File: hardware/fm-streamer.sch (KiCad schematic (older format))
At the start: 35 parts

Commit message: schematics nominally finished, moving on to PCB
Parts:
- removed C?: 0.1u, symbol Device:C_Small
- removed C? (x5): 10u, symbol Device:C_Small
- removed C? (x2): 47u, symbol Device:CP_Small
- removed R? (x6): 10k, symbol Device:R_Small
- removed U?: ESP32-DEVKITC-32D, MODULE_ESP32-DEVKITC-32D, symbol ESP32-DEVKITC-32D:ESP32-DEVKITC-32D
- removed U?: UDA1334ATS, Package_SO:SSOP-16_4.4x5.2mm_P0.65mm, symbol Audio:UDA1334ATS
- added C1: 0.1u, Capacitor_SMD:C_0402_1005Metric, symbol Device:C_Small
- added C10, C11, C17, C4, C5, C6, C7, C8, C9: 22n, Capacitor_SMD:C_0402_1005Metric, symbol Device:C_Small
- added C12, C14, C16, C19, C2, C20, C22, C23, C3: 10u, Capacitor_SMD:C_0603_1608Metric, symbol Device:C_Small
- added J1: USB_A, Connector_USB:USB_A_Molex_105057_Vertical, symbol Connector:USB_A
- added L1: 120n, Inductor_SMD:L_0603_1608Metric, symbol Device:L_Small
- added R1, R14, R2: 0, Resistor_SMD:R_0402_1005Metric, symbol Device:R_Small
- added R10, R11, R17, R7, R8, R9: 100, Resistor_SMD:R_0402_1005Metric, symbol Device:R_Small
- added R15, R16, R20, R21: 10k, Resistor_SMD:R_0402_1005Metric, symbol Device:R_Small
- added TP1: TestPoint, TestPoint:TestPoint_Plated_Hole_D2.0mm, symbol Connector:TestPoint
- added U1: ESP32_DevKit_V1_DOIT, esp32_devkit_v1_doit:esp32_devkit_v1_doit, symbol esp32_devkit_v1_doit:ESP32_DevKit_V1_DOIT
- added U2: PCM1772PWR, footprints:PCM1772PWR, symbol 2021-05-02_19-16-46:PCM1772PWR
- C13, C15, C18: renamed from C?; footprint (none) -> Capacitor_SMD:C_0402_1005Metric; MFG (none) -> Murata; MPN (none) -> GCM155R71C104KA55J
- C21: renamed from C?; footprint (none) -> Capacitor_SMD:C_0603_1608Metric; MFG (none) -> Murata; MPN (none) -> GRT188C81A106ME13D
- R12, R13, R18, R19, R22, R23, R24, R25, R26, R27, R3, R4, R5, R6: renamed from R?; footprint (none) -> Resistor_SMD:R_0402_1005Metric
- U3: renamed from U?; footprint QFN-20-3X3MM -> SI4721:QFN-20-3X3MM; MFG (none) -> Silicon Labs; MPN (none) -> SI4721-B20-GM
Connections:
- net +3V3: now also R13.2, C14.1, C17.1, C3.2, U1.16 (3V3), U2.12 (VCC1); no longer R13.1
- net AUDIO_L: now also R27.1, C23.1; no longer R26.1
- net AUDIO_R: now also R26.1, C22.2; no longer R27.1
- net GND: now also U3.2 (FMI), C1.2, C10.2, C11.2, C12.2, C14.2, C16.2, C17.2, C2.2, C22.1, C23.2, C3.1, C4.2, C5.2, C6.2, C7.2, C8.2, C9.2, J1.4 (GND), J1.5 (Shield), L1.2, R1.1, R15.2, R16.2, R17.2, R2.1, R20.2, R21.2, U1.14 (GND), U1.17 (GND), U2.5 (AGND1), U2.6 (AGND2)
- net I2C_SCK: now also U1.29 (IO22)
- net I2C_SDA: now also U1.26 (IO21)
- net I2S_DATA: now also C5.1, U2.2 (DATA)
- net I2S_DCLK: now also C6.1, U2.3 (BCK)
- net I2S_WCLK: now also C4.1, U2.1 (LRCK)
- net RADIO_~RST~: now also U1.8 (IO25)
- net at U3.18 (GPO2/~INT): now also R21.1
- net at U3.19 (GPO1): now also R20.1
- net at U3.4 (TXO): now also L1.1, R14.1, TP1.1
- net RADIO_REFCLK: now reaches U3.9 (RCLK)
- net RADIO_REFCLK: now also C7.1, R7.1
- net at C13.1: now also R13.1, C12.1, U2.11 (VCC2); no longer R13.2
- net at R25.2, R27.2: now also C20.1
- net at R24.1, R26.2: now also C19.1
- net I2S_WCLK_R: now reaches R4.2
- net I2S_WCLK_R: now also U1.22 (IO17)
- net I2S_DATA_R: now reaches R5.2
- net I2S_DATA_R: now also U1.21 (IO16)
- net I2S_DCLK_R: now reaches R6.2
- net I2S_DCLK_R: now also U1.20 (IO4)
- new net: J1.2 (D-), R2.2
- new net: J1.3 (D+), R1.2
- new net: R17.1, U2.10 (AIN)
- new net: C16.1, U2.7 (VCOM)
- new net: C19.2, U2.8 (VOUTR)
- new net: C20.2, U2.9 (VOUTL)
- new net +5V: C1.1, C2.1, J1.1 (VBUS), U1.15 (VIN)
- new net ANTENNA: R14.2
- new net DAC_CLK_R: R8.2, U1.28 (TXD0/IO1)
- new net DAC_REFCLK: C8.1, R8.1, U2.16 (SCKI)
- new net DAC_~RST~: R15.1, U1.10 (IO27), U2.4 (*PD)
- new net RAD_CLK_R: R7.2, U1.27 (RXD0/IO3)
- new net SPI_CLK: C10.1, R10.1, U2.14 (MC)
- new net SPI_CLK_R: R10.2, U1.24 (IO18)
- new net SPI_CS: C11.1, R11.1
- new net SPI_CS_R: R11.2, U1.23 (IO5)
- new net SPI_MOSI: C9.1, R9.1, U2.13 (MD)
- new net SPI_MOSI_R: R9.2, U1.30 (IO23)
- new net SPI_~CS~: R16.1, U2.15 (*MS)
- no-connect marks 1 -> 3
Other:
- note added: "Testpoint for optional wire antenna"
- note added: "http://esp32.net/images/DOIT/ESP32-DevKit-V1/DOIT_ESP32-DevKit_Schematic.pdf"
- moved on the sheet: C13, C15, C18, C21, R12, R13, R18, R19, R22, R23, R24, R25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

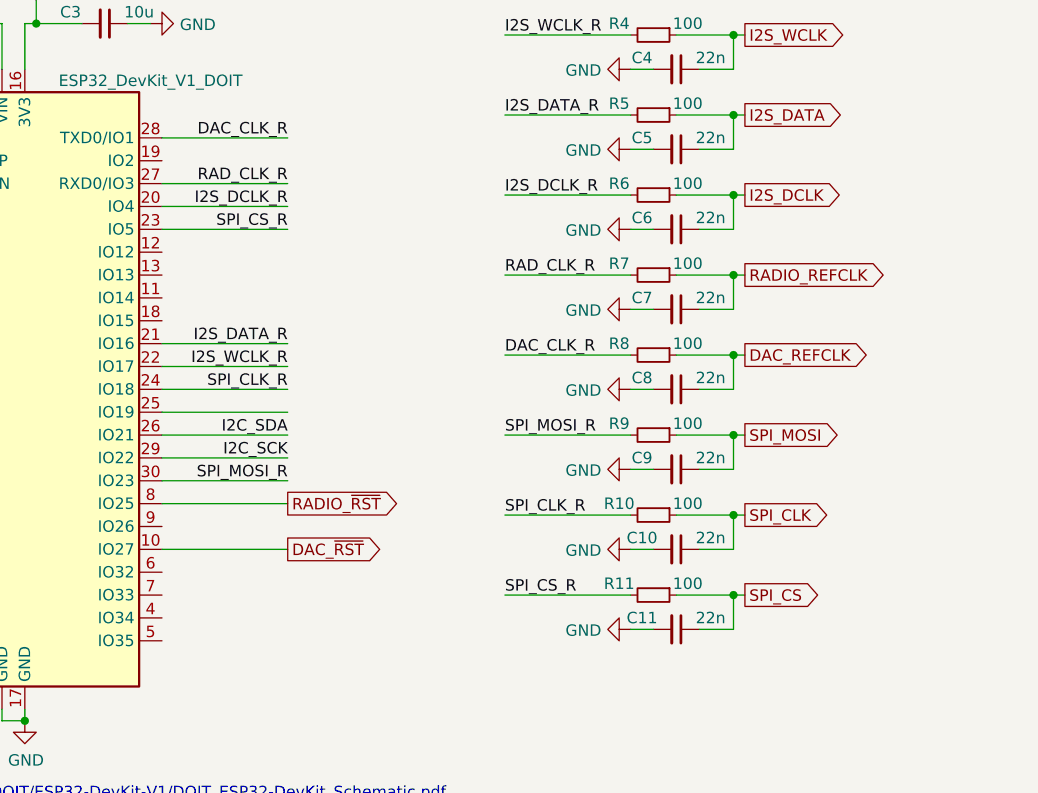
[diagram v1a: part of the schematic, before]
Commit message: rough placement and routing complete, needs cleanup
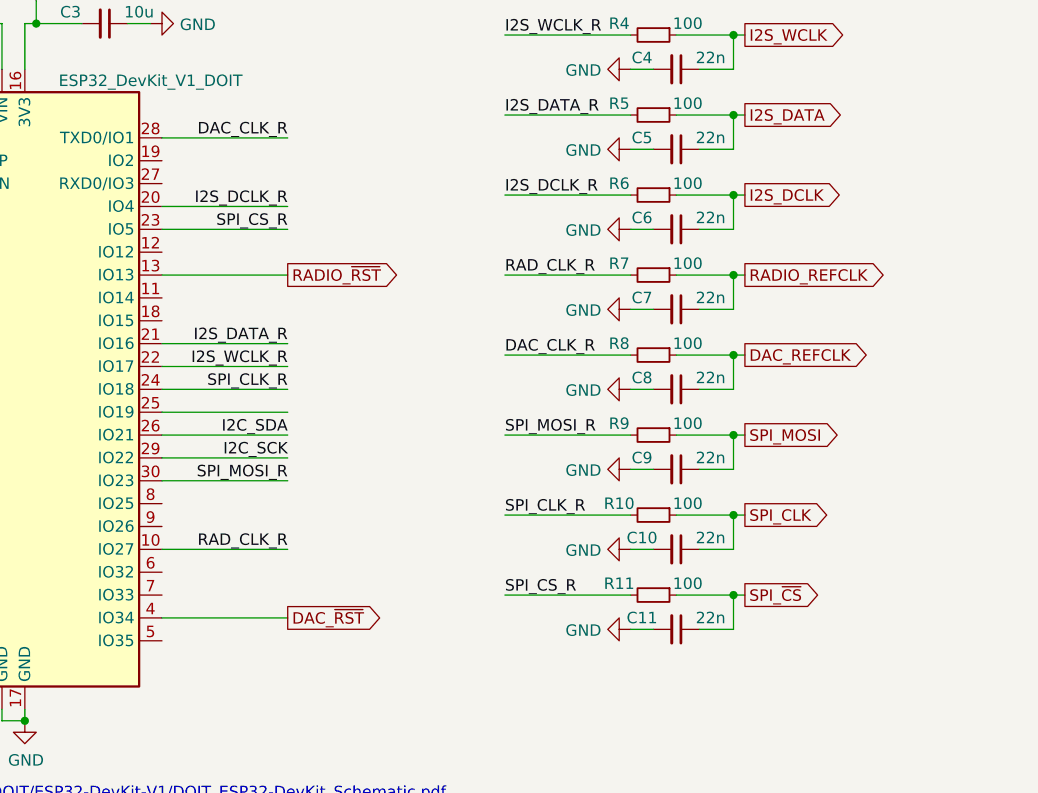
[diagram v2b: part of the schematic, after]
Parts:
- TP1: footprint TestPoint:TestPoint_Plated_Hole_D2.0mm -> TestPoint:TestPoint_THTPad_D2.0mm_Drill1.0mm
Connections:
- net SPI_CS is gone; now on net SPI_~CS~: C11.1, R11.1
- net DAC_~RST~: now also U1.4 (IO34); no longer U1.10 (IO27)
- net RADIO_~RST~: now also U1.13 (IO13); no longer U1.8 (IO25)
- net RAD_CLK_R: now also U1.10 (IO27); no longer U1.27 (RXD0/IO3)
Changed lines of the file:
@@
 Text GLabel 7400 2950 2    50   BiDi ~ 0
 I2C_SDA
-Text GLabel 5400 5350 2    50   Output ~ 0
+Text GLabel 5400 4350 2    50   Output ~ 0
 RADIO_~RST~
 $Comp
@@
 F 0 "TP1" H 10108 3272 50  0000 L CNN
 F 1 "TestPoint" H 10108 3227 50  0001 L CNN
-F 2 "TestPoint:TestPoint_Plated_Hole_D2.0mm" H 10250 3200 50  0001 C CNN
+F 2 "TestPoint:TestPoint_THTPad_D2.0mm_Drill1.0mm" H 10250 3200 50  0001 C CNN
 F 3 "~" H 10250 3200 50  0001 C CNN
 F 4 "~" H 10050 3200 50  0001 C CNN "MFG"
@@
 	4850 5150 5400 5150
 Wire Wire Line
-	5400 5350 4850 5350
+	5400 4350 4850 4350
 Wire Wire Line
 	6900 4000 6350 4000
@@
 Text Label 6350 4350 0    50   ~ 0
 RAD_CLK_R
-Text Label 5400 3950 2    50   ~ 0
+Text Label 5400 5550 2    50   ~ 0
 RAD_CLK_R
 Wire Wire Line
-	5400 3950 4850 3950
+	5400 5550 4850 5550
 Connection ~ 7350 4350
 Wire Wire Line
@@
 	7350 5750 7400 5750
 Text GLabel 7400 5750 2    50   Output ~ 0
-SPI_CS
+SPI_~CS~
 Text Label 5400 5250 2    50   ~ 0
 SPI_MOSI_R
@@
 Text Label 5400 4150 2    50   ~ 0
 SPI_CS_R
-Text GLabel 5400 5550 2    50   Output ~ 0
+Text GLabel 5400 5850 2    50   Output ~ 0
 DAC_~RST~
 Wire Wire Line
-	4850 5550 5400 5550
+	4850 5850 5400 5850
 $Comp
 L Device:C_Small C19

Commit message: cleaning up routing
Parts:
- added R28, R29, R30: 0, Resistor_SMD:R_0402_1005Metric, symbol Device:R_Small
- J1: footprint Connector_USB:USB_A_Molex_105057_Vertical -> Connector_USB:USB_A_Plug_Molex_0480371000_90_deg_mount
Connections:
- net DAC_CLK_R: now also U1.4 (IO34); no longer U1.28 (TXD0/IO1)
- net DAC_~RST~: now also U1.26 (IO21); no longer U1.4 (IO34)
- net I2C_SDA: now also U1.9 (IO26); no longer U1.26 (IO21)
- net I2S_DATA: now also R29.2; no longer U2.2 (DATA)
- net I2S_DATA_R: now also U1.24 (IO18); no longer U1.21 (IO16)
- net I2S_DCLK: now also R28.2; no longer U2.3 (BCK)
- net I2S_DCLK_R: now also U1.21 (IO16); no longer U1.20 (IO4)
- net I2S_WCLK: now also R30.2; no longer U2.1 (LRCK)
- net RAD_CLK_R: now also U1.8 (IO25); no longer U1.10 (IO27)
- net SPI_CLK_R: now also U1.6 (IO32); no longer U1.24 (IO18)
- net SPI_CS_R: now also U1.5 (IO35); no longer U1.23 (IO5)
- net SPI_MOSI_R: now also U1.7 (IO33); no longer U1.30 (IO23)
- net I2C_SCK renamed I2C_SCL
- net I2C_SCL: now also U1.10 (IO27); no longer U1.29 (IO22)
- new net: R30.1, U2.1 (LRCK)
- new net: R29.1, U2.2 (DATA)
- new net: R28.1, U2.3 (BCK)
- no-connect marks 3 -> 10
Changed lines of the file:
@@
 	9550 7200 9550 7150
 Wire Wire Line
-	11500 6150 10700 6150
-Wire Wire Line
-	11500 6350 10700 6350
-Wire Wire Line
-	11500 6250 10700 6250
+	11500 6150 11300 6150
+Wire Wire Line
+	11500 6350 11300 6350
+Wire Wire Line
+	11500 6250 11300 6250
 $Comp
 L Device:R_Small R13
@@
 I2C_SDA
 Text GLabel 11250 3850 0    50   BiDi ~ 0
-I2C_SCK
+I2C_SCL
 Wire Wire Line
 	11250 3950 11800 3950
@@
 	7100 3300 7350 3300
 Text GLabel 7400 2850 2    50   BiDi ~ 0
-I2C_SCK
+I2C_SCL
 Text GLabel 7400 2950 2    50   BiDi ~ 0
 I2C_SDA
-Text GLabel 5400 4350 2    50   Output ~ 0
-RADIO_~RST~
 $Comp
 L Device:R_Small R18
@@
 F 0 "J1" H 2057 5317 50  0000 C CNN
 F 1 "USB_A" H 2057 5226 50  0000 C CNN
-F 2 "Connector_USB:USB_A_Molex_105057_Vertical" H 2150 4800 50  0001 C CNN
+F 2 "Connector_USB:USB_A_Plug_Molex_0480371000_90_deg_mount" H 2150 4800 50  0001 C CNN
 F 3 " ~" H 2150 4800 50  0001 C CNN
 	1    2000 4850
@@
 NoConn ~ 3650 3850
 NoConn ~ 3650 3950
-Text Label 5400 5150 2    50   ~ 0
-I2C_SCK
+Text Label 5400 5550 2    50   ~ 0
+I2C_SCL
 Text Label 6450 2850 0    50   ~ 0
-I2C_SCK
+I2C_SCL
 Wire Wire Line
 	6450 2850 7250 2850
@@
 Text Label 6450 2950 0    50   ~ 0
 I2C_SDA
-Text Label 5400 5050 2    50   ~ 0
-I2C_SDA
-Wire Wire Line
-	4850 5050 5400 5050
-Wire Wire Line
-	4850 5150 5400 5150
-Wire Wire Line
-	5400 4350 4850 4350
+Wire Wire Line
+	4850 5550 5400 5550
 Wire Wire Line
 	6900 4000 6350 4000
@@
 Text Label 6350 4000 0    50   ~ 0
 I2S_DCLK_R
-Text Label 5400 4050 2    50   ~ 0
-I2S_DCLK_R
-Wire Wire Line
-	5400 4050 4850 4050
-Text Label 5400 4650 2    50   ~ 0
+Text Label 5400 4850 2    50   ~ 0
 I2S_DATA_R
 Wire Wire Line
-	5400 4650 4850 4650
+	5400 4850 4850 4850
 Text Label 5400 4750 2    50   ~ 0
 I2S_WCLK_R
@@
 Text Label 6350 4350 0    50   ~ 0
 RAD_CLK_R
-Text Label 5400 5550 2    50   ~ 0
+Text Label 5400 5350 2    50   ~ 0
 RAD_CLK_R
 Wire Wire Line
-	5400 5550 4850 5550
+	5400 5350 4850 5350
 Connection ~ 7350 4350
 Wire Wire Line
@@
 Text GLabel 7400 4700 2    50   Output ~ 0
 DAC_REFCLK
-Text Label 5400 3750 2    50   ~ 0
+Text Label 5400 5850 2    50   ~ 0
 DAC_CLK_R
 Wire Wire Line
-	4850 3750 5400 3750
-Wire Wire Line
-	4850 5250 5400 5250
-Wire Wire Line
-	4850 4950 5400 4950
-Wire Wire Line
-	4850 4850 5400 4850
-Wire Wire Line
-	4850 4150 5400 4150
+	4850 5850 5400 5850
+Wire Wire Line
+	4850 5750 5400 5750
+Wire Wire Line
+	4850 5650 5400 5650
+Wire Wire Line
+	4850 5950 5400 5950
 $Comp
 L Device:R_Small R9
@@
 Text GLabel 7400 5750 2    50   Output ~ 0
 SPI_~CS~
-Text Label 5400 5250 2    50   ~ 0
+Text Label 5400 5750 2    50   ~ 0
 SPI_MOSI_R
-Text Label 5400 4850 2    50   ~ 0
+Text Label 5400 5650 2    50   ~ 0
 SPI_CLK_R
-Text Label 5400 4150 2    50   ~ 0
-SPI_CS_R
-Text GLabel 5400 5850 2    50   Output ~ 0
-DAC_~RST~
-Wire Wire Line
-	4850 5850 5400 5850
 $Comp
 L Device:C_Small C19
@@
 Wire Wire Line
 	13400 6000 13400 5950
+Text Label 5400 5950 2    50   ~ 0
+SPI_CS_R
+Wire Wire Line
+	5400 4650 4850 4650
+Text Label 5400 4650 2    50   ~ 0
+I2S_DCLK_R
+NoConn ~ 4850 3850
+NoConn ~ 4850 4050
+NoConn ~ 4850 4150
+NoConn ~ 4850 4250
+NoConn ~ 4850 4550
+NoConn ~ 4850 3750
+NoConn ~ 4850 4450
+Wire Wire Line
+	5400 4350 4850 4350
+Text GLabel 5400 4350 2    50   Output ~ 0
+RADIO_~RST~
+Wire Wire Line
+	4850 5450 5400 5450
+Text Label 5400 5450 2    50   ~ 0
+I2C_SDA
+$Comp
+L Device:R_Small R28
+U 1 1 61682B52
+P 11200 6150
+F 0 "R28" V 11150 6000 50  0000 C CNN
+F 1 "0" V 11150 6300 50  0000 C CNN
+F 2 "Resistor_SMD:R_0402_1005Metric" H 11200 6150 50  0001 C CNN
+F 3 "~" H 11200 6150 50  0001 C CNN
+	1    11200 6150
+	0    1    1    0
+$EndComp
+Wire Wire Line
+	11100 6150 10700 6150
+$Comp
+L Device:R_Small R29
+U 1 1 61683E88
+P 11200 6250
+F 0 "R29" V 11150 6100 50  0000 C CNN
+F 1 "0" V 11150 6400 50  0000 C CNN
+F 2 "Resistor_SMD:R_0402_1005Metric" H 11200 6250 50  0001 C CNN
+F 3 "~" H 11200 6250 50  0001 C CNN
+	1    11200 6250
+	0    1    1    0
+$EndComp
+Wire Wire Line
+	11100 6250 10700 6250
+$Comp
+L Device:R_Small R30
+U 1 1 61684267
+P 11200 6350
+F 0 "R30" V 11150 6200 50  0000 C CNN
+F 1 "0" V 11150 6500 50  0000 C CNN
+F 2 "Resistor_SMD:R_0402_1005Metric" H 11200 6350 50  0001 C CNN
+F 3 "~" H 11200 6350 50  0001 C CNN
+	1    11200 6350
+	0    1    1    0
+$EndComp
+Wire Wire Line
+	11100 6350 10700 6350
+Wire Wire Line
+	4850 5050 5400 5050
+Text GLabel 5400 5050 2    50   Output ~ 0
+DAC_~RST~
 $EndSCHEMATC

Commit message: Rev0 out to fab
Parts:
- J1: MFG (none) -> Molex; MPN (none) -> 0480371000
- R1, R14, R2, R28, R29, R30: MFG (none) -> Stackpole; MPN (none) -> RMCF0402ZT0R00
- R10, R11, R17, R22, R23, R26, R27, R4, R5, R6, R7, R8, R9: MFG (none) -> Panasonic; MPN (none) -> ERJ-2RKF1000X
- R12, R3: MFG (none) -> Panasonic; MPN (none) -> ERJ-2RKF4701X
- R13: MFG (none) -> Panasonic; MPN (none) -> ERJ-2BQJ1R0X
- R15, R16, R18, R19, R20, R21: MFG (none) -> Panasonic; MPN (none) -> ERJ-2RKF1002X
- R24, R25: MFG (none) -> Panasonic; MPN (none) -> ERJ-2RKF2203X
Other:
- note added: "ESP32 Dev Kit Module"
- note added: "FM Radio Transmitter\n"
- note added: "I2S Audio DAC"
- moved on the sheet: C1, C10, C11, C12, C13, C14, C15, C16, C17, C18, C19, C2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
